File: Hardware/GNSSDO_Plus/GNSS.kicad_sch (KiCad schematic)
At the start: 36 parts, among them J1 SMA_Edge, J6 microSD, U2 mosaic-T

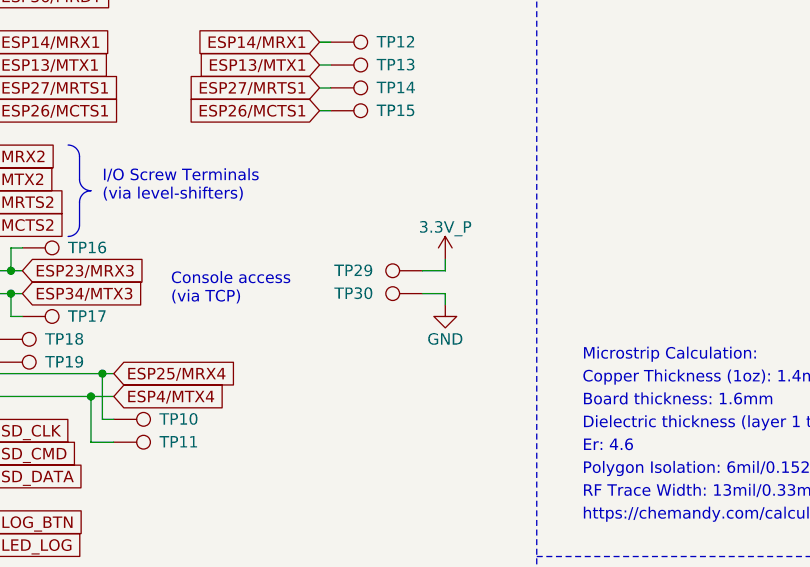
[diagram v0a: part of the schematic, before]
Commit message: GNSSDO Plus: add 3-way splitter
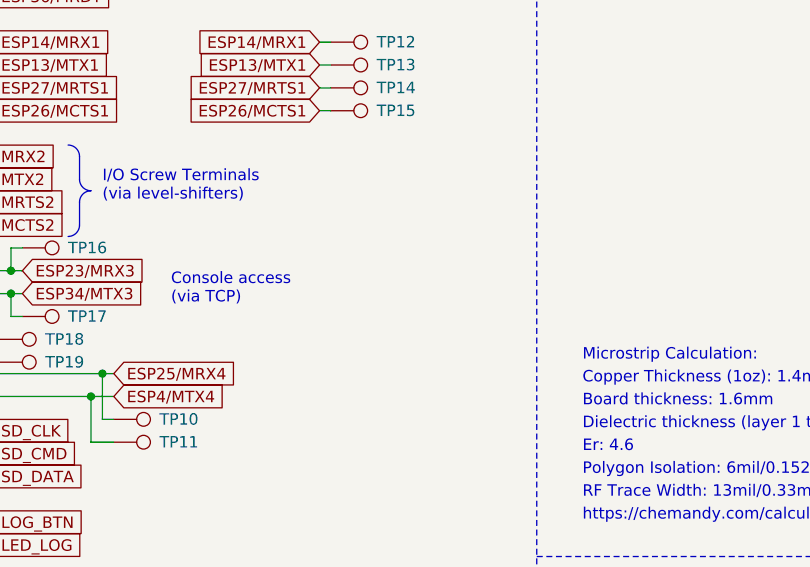
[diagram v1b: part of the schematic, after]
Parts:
- removed TP29, TP30: PTH, SparkFun-Connector:1x01, symbol SparkFun-Connector:TestPoint_PTH

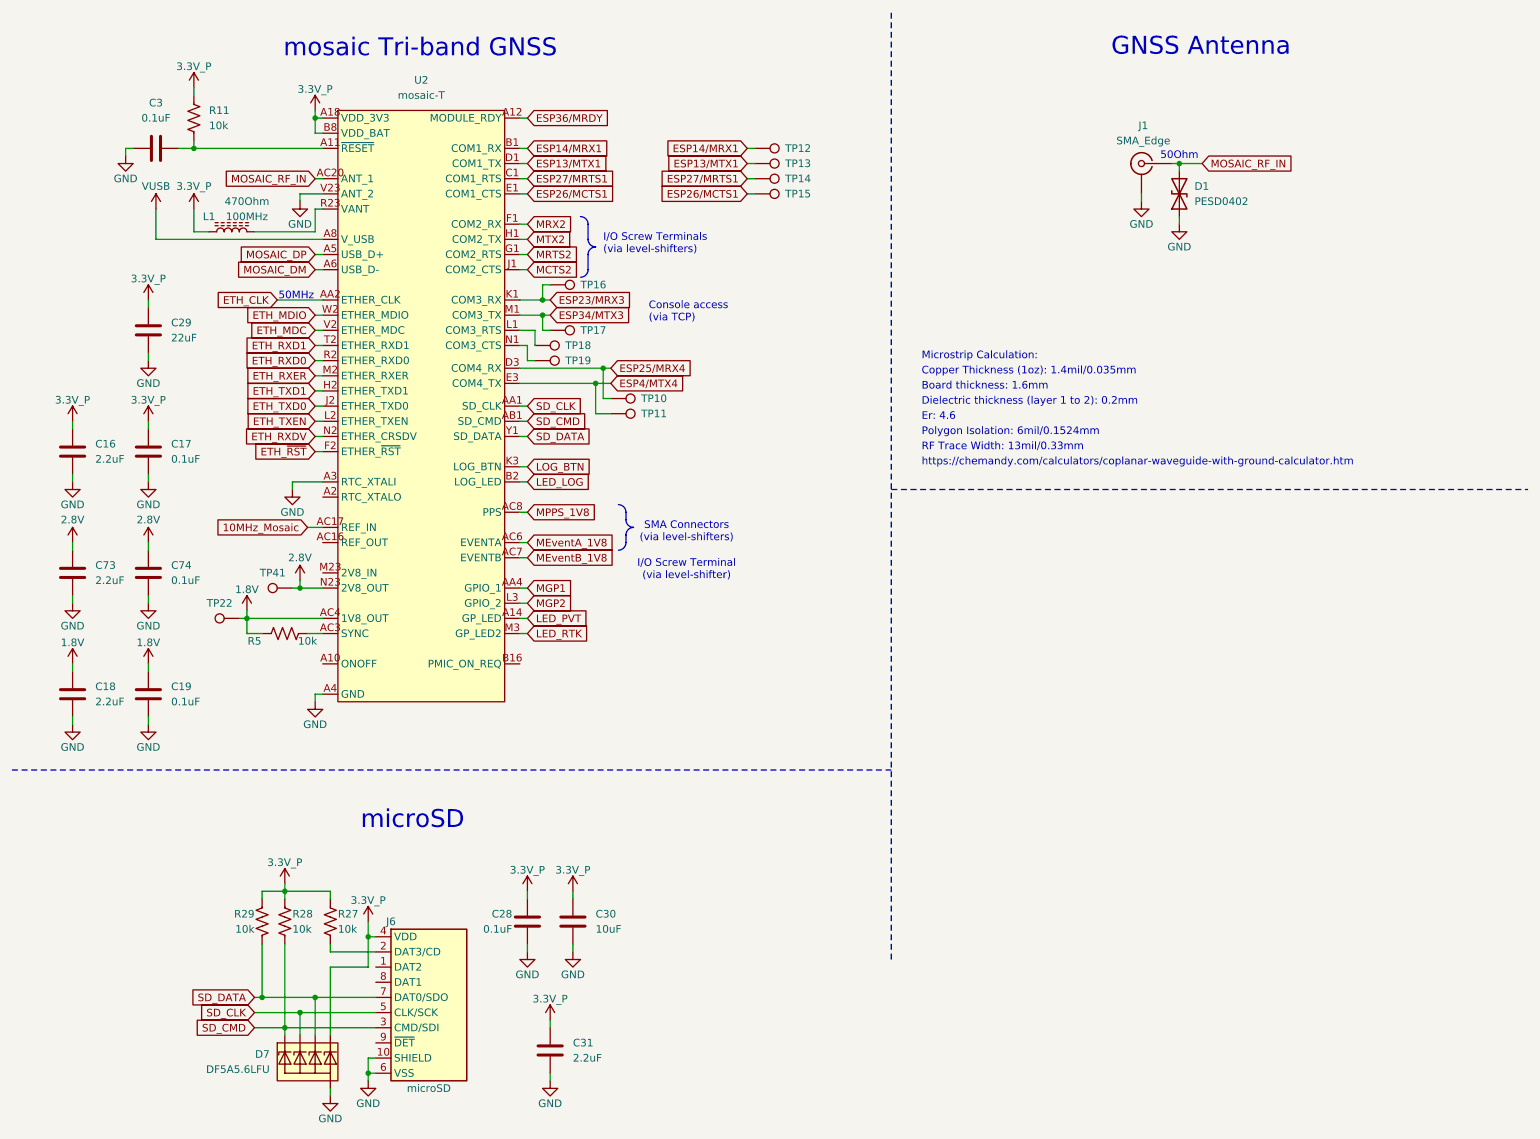
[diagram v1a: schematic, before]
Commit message: GNSSDO+ : update symbols and footprints
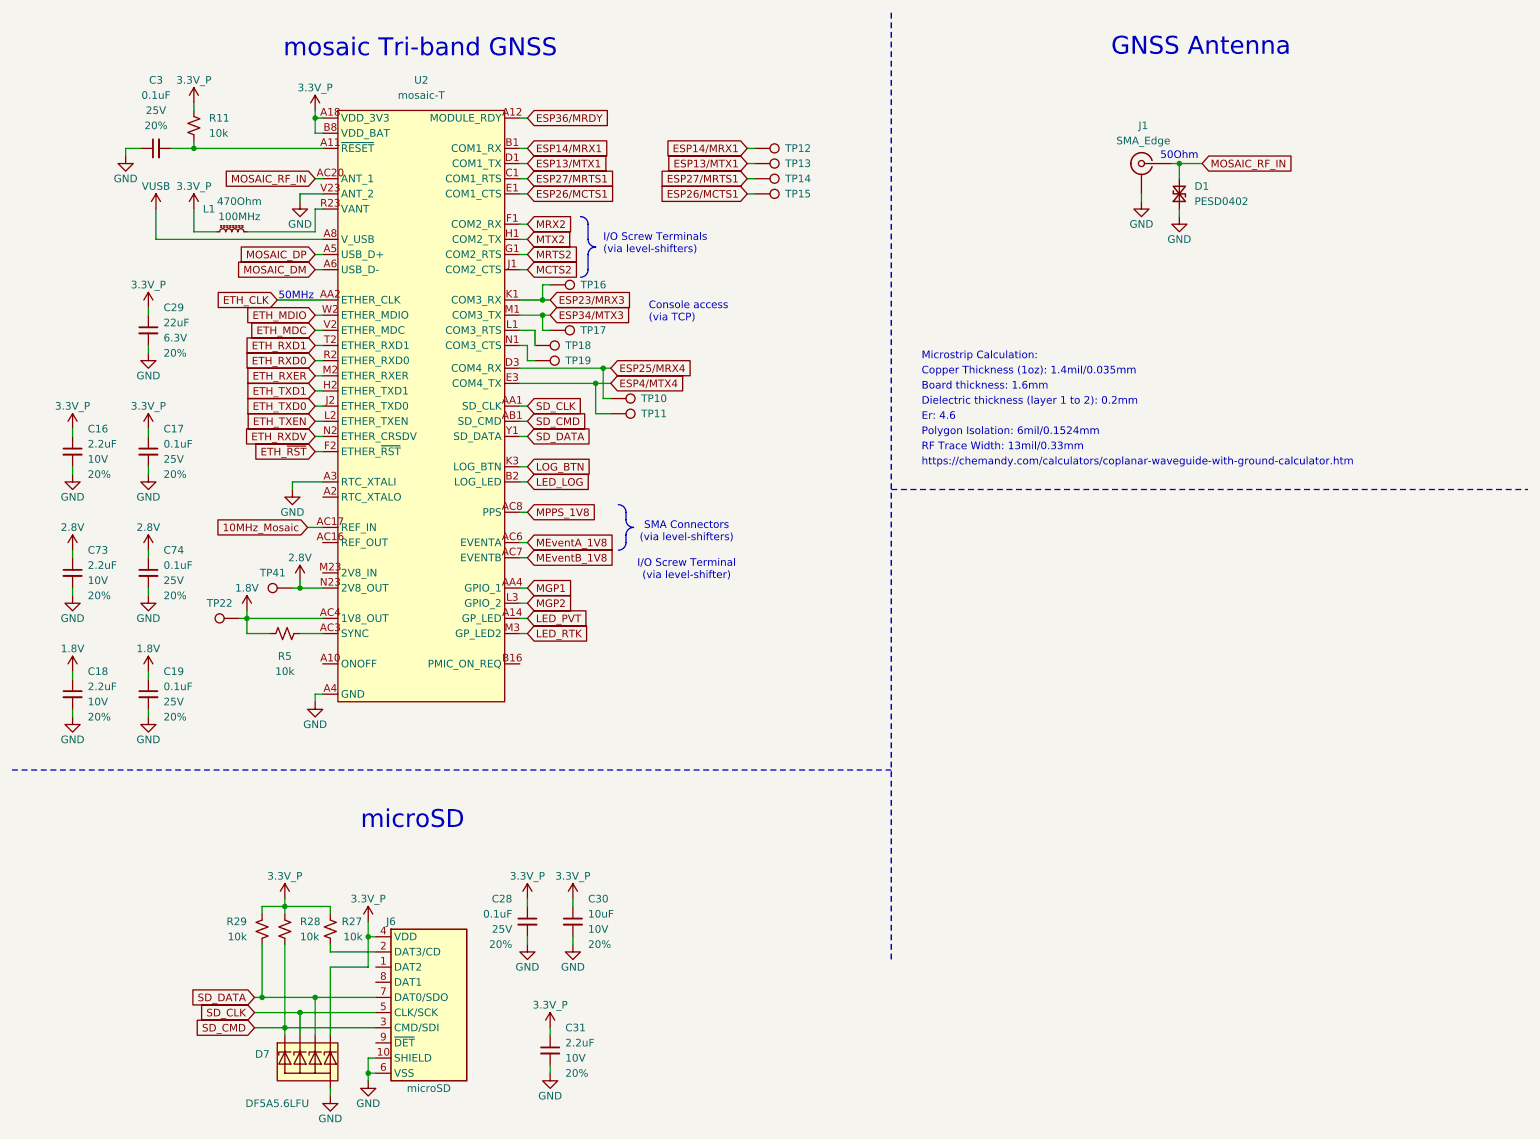
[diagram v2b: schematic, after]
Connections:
- net 1.8V: now also R5.1; no longer R5.2
- net 3.3V_P: now also R11.1, R27.1, R28.1, R29.1; no longer R11.2, R27.2, R28.2, R29.2
- net SD_CMD: now also R28.2; no longer R28.1
- net SD_DATA: now also R29.2; no longer R29.1
- net at C3.2, U2.A11 (~{RESET}): now also R11.2; no longer R11.1
- net at U2.AC3 (SYNC): now also R5.2; no longer R5.1
- net at J6.2 (DAT3/CD): now also R27.2; no longer R27.1

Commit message: GNSSDO Plus - ready for review
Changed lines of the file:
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@@
+	(text "I/O Screw Terminals\n(via level-shifters)"
+		(exclude_from_sim no)
+		(at 118.11 112.395 0)
+		(effects
+			(font
+				(size 1.27 1.27)
+			)
+			(justify bottom)
+		)
+	)
 	(text "I/O Screw Terminals\n(via level-shifters)"
 		(exclude_from_sim no)
@@
 	(text "I/O Screw Terminal\n(via level-shifter)"
 		(exclude_from_sim no)
-		(at 125.73 107.95 0)
+		(at 125.73 107.315 0)
 		(effects
 			(font

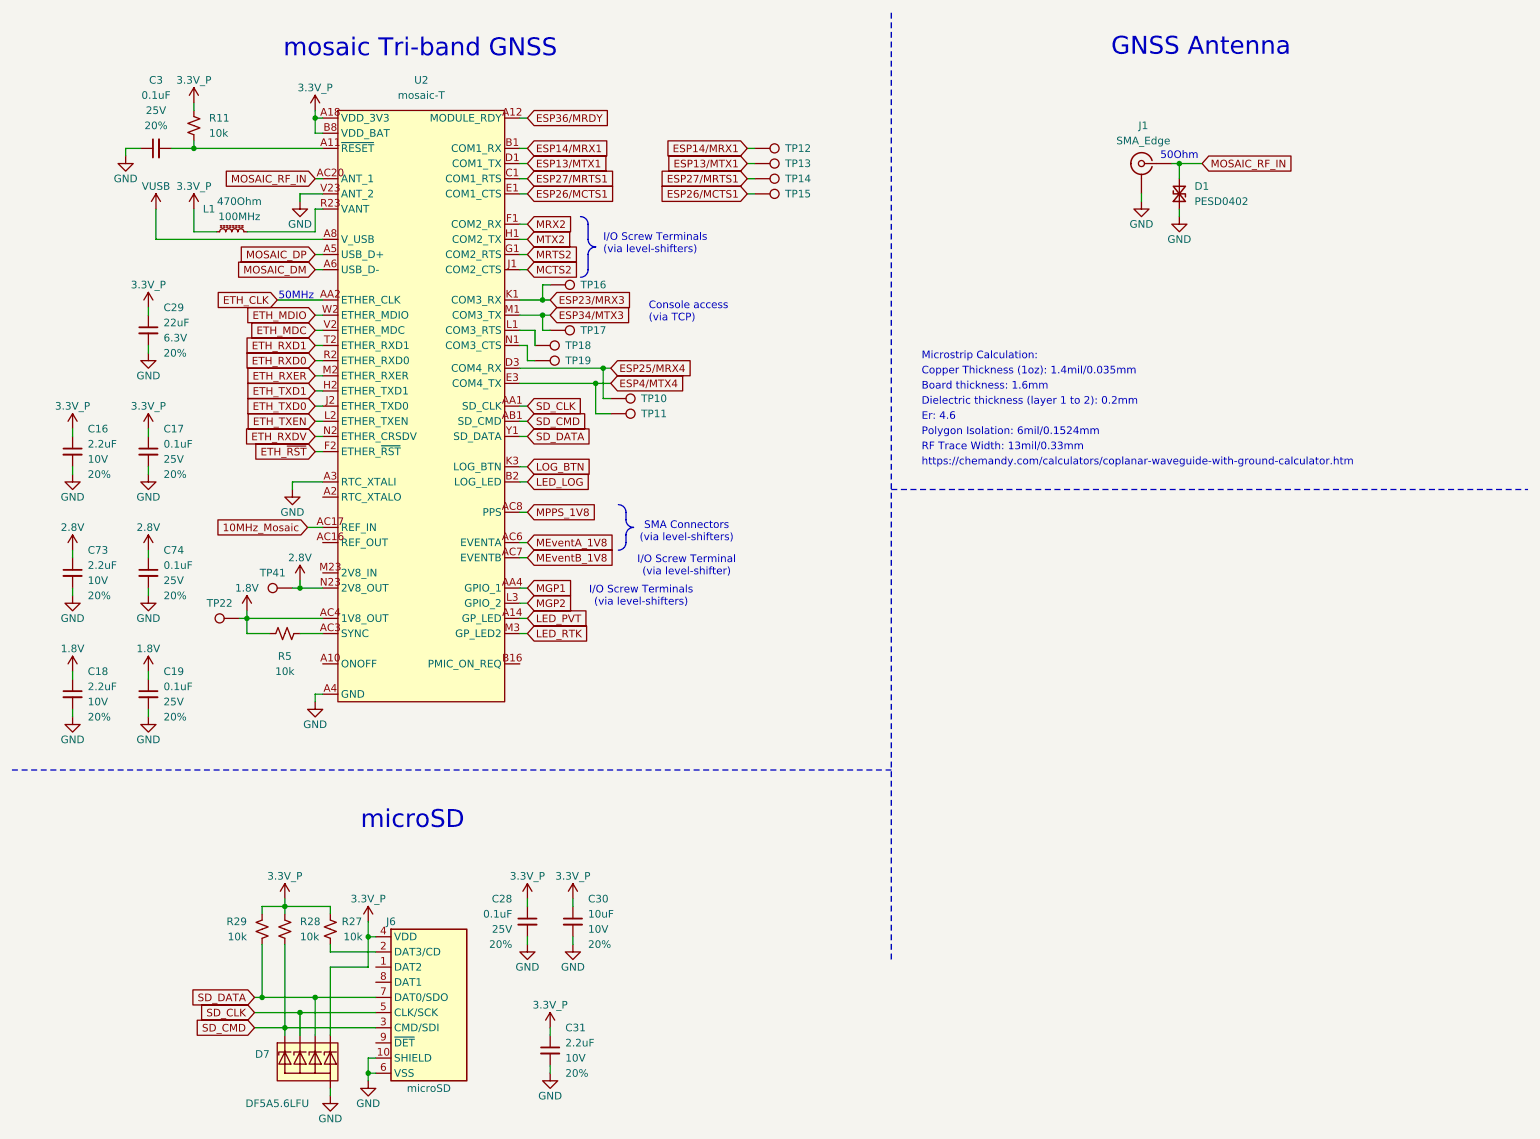
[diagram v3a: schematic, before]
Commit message: GNSSDO+ v02 PCB - with DP5305 PoE module, PowerPath Controllers and MS8607 PHT sensor
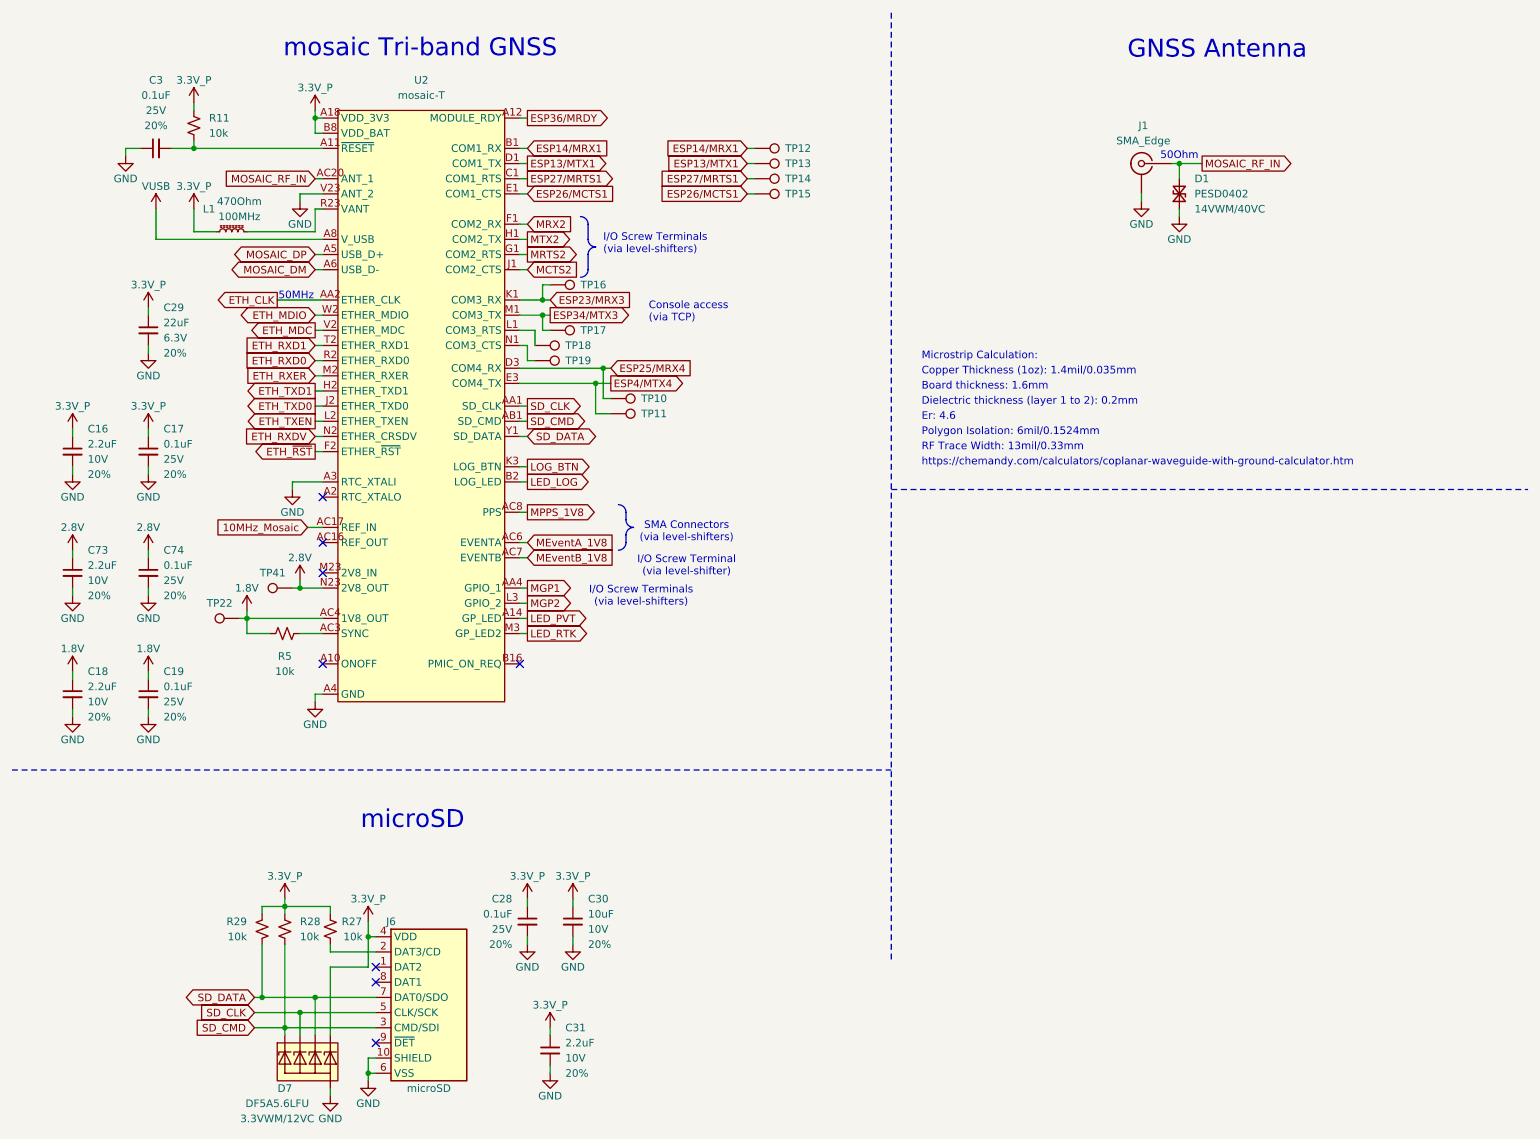
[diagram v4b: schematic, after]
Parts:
- D1: symbol SparkFun-DiscreteSemi:D_TVS_0402 -> SparkFun-DiscreteSemi:D_TVS_0402_14V; Rating (none) -> 14VWM/40VC
- D7: symbol SparkFun-DiscreteSemi:D_TVS_ESD_4_HS -> SparkFun-DiscreteSemi:D_TVS_ESD_4_HS_3.3V; Rating (none) -> 3.3VWM/12VC
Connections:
- no-connect marks 0 -> 8
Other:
- title: GNSS -> GNSSDO Plus - GNSS

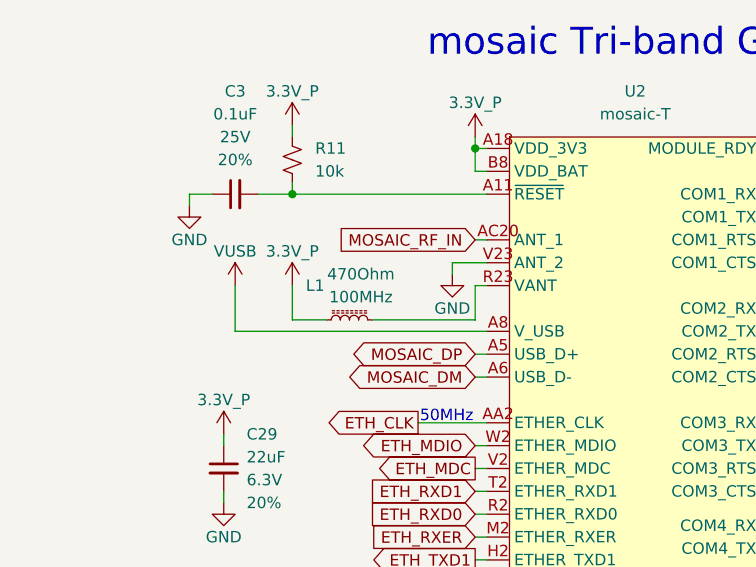
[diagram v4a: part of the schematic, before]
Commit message: Update GNSSDO KiCad files to match latest SparkFun library
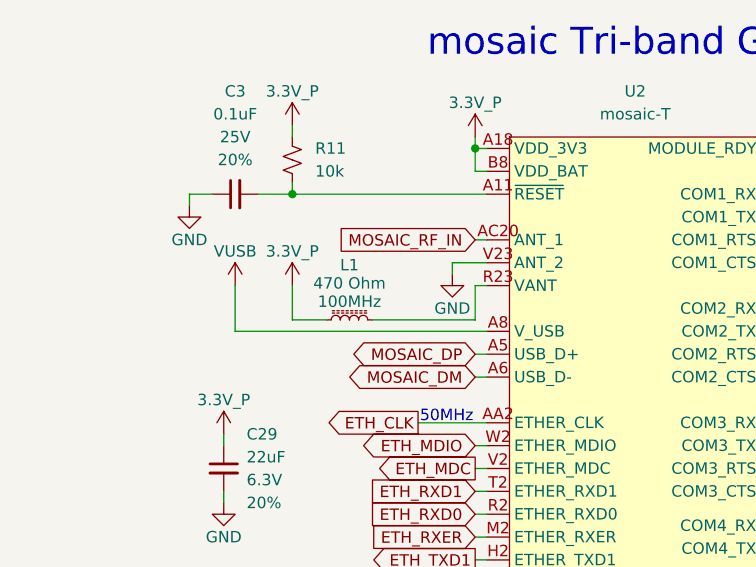
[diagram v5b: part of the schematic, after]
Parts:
- C16, C18, C31, C73: PROD_ID CAP-07888 -> CAP-24999
- J1: footprint SparkFun-Connector:SMA_Edge -> SparkFun-Connector:SMA_Edge_6.3mm; symbol SparkFun-RF:SMA_EdgeMount -> SparkFun-RF:SMA_EdgeMount_6.3mm
- L1: value 470Ohm -> 470 Ohm; symbol SparkFun-Coil:470Ohm_0603_1.0A -> SparkFun-Coil:Ferrite_470Ohm_0603_1.0A
- TP10, TP11, TP12, TP13, TP14, TP15, TP16, TP17, TP18, TP19, TP22, TP41: footprint SparkFun-Connector:1x01 -> SparkFun-Connector:1x01_P2.54mm
- U2: footprint SparkFun-GPS:MOSAIC_LGA -> SparkFun-GNSS:Septentrio_mosaic_LGA; symbol SparkFun-GPS:mosaic-T -> SparkFun-GNSS:mosaic-T
